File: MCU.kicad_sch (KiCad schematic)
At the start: 3 parts, among them U1 ESP32-S2-SOLO-N4

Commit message: Completed first iteration and reviews
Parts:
- added GND1: TestPoint, TestPoint:TestPoint_Pad_D1.0mm, symbol Connector:TestPoint
- added J3: Conn_02x03_Odd_Even, Connector_PinHeader_1.27mm:PinHeader_2x03_P1.27mm_Vertical_SMD, symbol Connector_Generic:Conn_02x03_Odd_Even
- added R2, R5: 10k, Resistor_SMD:R_0805_2012Metric_Pad1.20x1.40mm_HandSolder, symbol Device:R
- C1: footprint (none) -> Capacitor_SMD:C_0805_2012Metric_Pad1.18x1.45mm_HandSolder; Supplier (none) -> Digikey; Supplier Part Number (none) -> 1276-CL21A226MAYNNNECT-ND
- C2: footprint (none) -> Capacitor_SMD:C_0805_2012Metric_Pad1.18x1.45mm_HandSolder; Supplier (none) -> Digikey; Supplier Part Number (none) -> 1276-1003-1-ND
- U1: value ESP32-S2-SOLO-N4 -> ESP32-S2-SOLO-2-N4; footprint ESP32-S2-SOLO-N4:XCVR_ESP32-S2-SOLO-N4 -> Hydro_footprints:ESP32-S2-SOLO-N4; Supplier (none) -> Digikey; Supplier Part Number (none) -> 1965-ESP32-S2-SOLO-2-N4CT-ND
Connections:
- net GND: now also GND1.1, J3.4 (Pin_4)
- net OP_AMP_POWER: now also U1.17 (IO9); no longer U1.6 (IO6)
- net SENSOR_OUTPUT: now also U1.18 (IO10); no longer U1.4 (IO4)
- net SENSOR_PWR: now also U1.19 (IO11); no longer U1.7 (IO7)
- net 3V3: now reaches C1.1, C2.1, U1.2 (3V3)
- net 3V3: now also J3.2 (Pin_2), R2.1, R5.1
- net QI_EN2: now reaches U1.10 (IO17)
- net CHARGE_STATUS: now reaches U1.11 (IO18)
- net Battery_Voltage: now reaches U1.12 (IO8)
- net ESP_BOOT: now reaches U1.27 (IO0)
- net ESP_BOOT: now also J3.6 (Pin_6), R5.2
- net ESP_EN: now reaches U1.3 (EN)
- net ESP_EN: now also J3.1 (Pin_1), R2.2
- net RXD0: now reaches U1.36 (RXD0)
- net RXD0: now also J3.5 (Pin_5)
- net TXD0: now reaches U1.37 (TXD0)
- net TXD0: now also J3.3 (Pin_3)
- no-connect marks 0 -> 27
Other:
- note added: "Ensure to pullup on MCU"
- company: (none) -> Horatio Pistachio
- title: (none) -> WashingLineMonitor-P0001
- moved on the sheet: C1, C2

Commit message: commit of local files before designing next version
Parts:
- J3: Digikey_Part_Number (none) -> SAM13920TR-ND; Part_Number SAM13920TR-ND -> (none)
- U1: JLC_Part_Number (none) -> C3040594
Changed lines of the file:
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@@
+			)
+		)
+		(property "JLC_Part_Number" ""
+			(at 175.26 77.47 0)
+			(effects
+				(font
+					(size 1.27 1.27)
+				)
+				(hide yes)
 			)
 		)
@@
 			)
 		)
-		(property "Part_Number" "SAM13920TR-ND"
-			(at 41.91 176.53 0)
-			(effects
-				(font
-					(size 1.27 1.27)
-				)
-				(hide yes)
-			)
-		)
 		(property "Supplier" "Digikey"
 			(at 41.91 176.53 0)
@@
 		)
 		(property "Supplier Part Number" "SAM13920TR-ND"
+			(at 41.91 176.53 0)
+			(effects
+				(font
+					(size 1.27 1.27)
+				)
+				(hide yes)
+			)
+		)
+		(property "Digikey_Part_Number" "SAM13920TR-ND"
+			(at 41.91 176.53 0)
+			(effects
+				(font
+					(size 1.27 1.27)
+				)
+				(hide yes)
+			)
+		)
+		(property "JLC_Part_Number" ""
 			(at 41.91 176.53 0)
 			(effects
@@
 			)
 		)
+		(property "JLC_Part_Number" ""
+			(at 105.41 63.5 0)
+			(effects
+				(font
+					(size 1.27 1.27)
+				)
+				(hide yes)
+			)
+		)
 		(pin "1"
 		)
@@
 			)
 		)
+		(property "JLC_Part_Number" "C3040594"
+			(at 125.73 96.52 0)
+			(effects
+				(font
+					(size 1.27 1.27)
+				)
+				(hide yes)
+			)
+		)
 		(pin "38"
 		)
@@
 			)
 		)
+		(property "JLC_Part_Number" ""
+			(at 82.55 64.77 0)
+			(effects
+				(font
+					(size 1.27 1.27)
+				)
+				(hide yes)
+			)
+		)
 		(pin "1"
 		)
@@
 			)
 		)
+		(property "JLC_Part_Number" ""
+			(at 149.86 124.46 0)
+			(effects
+				(font
+					(size 1.27 1.27)
+				)
+				(hide yes)
+			)
+		)
 		(pin "1"
 		)
@@
 			(at 187.96 77.47 0)
 			(effects
+				(font
+					(size 1.27 1.27)
+				)
+				(hide yes)
+			)
+		)
+		(property "JLC_Part_Number" ""
+			(at 187.96 77.47 0)
+			(effects

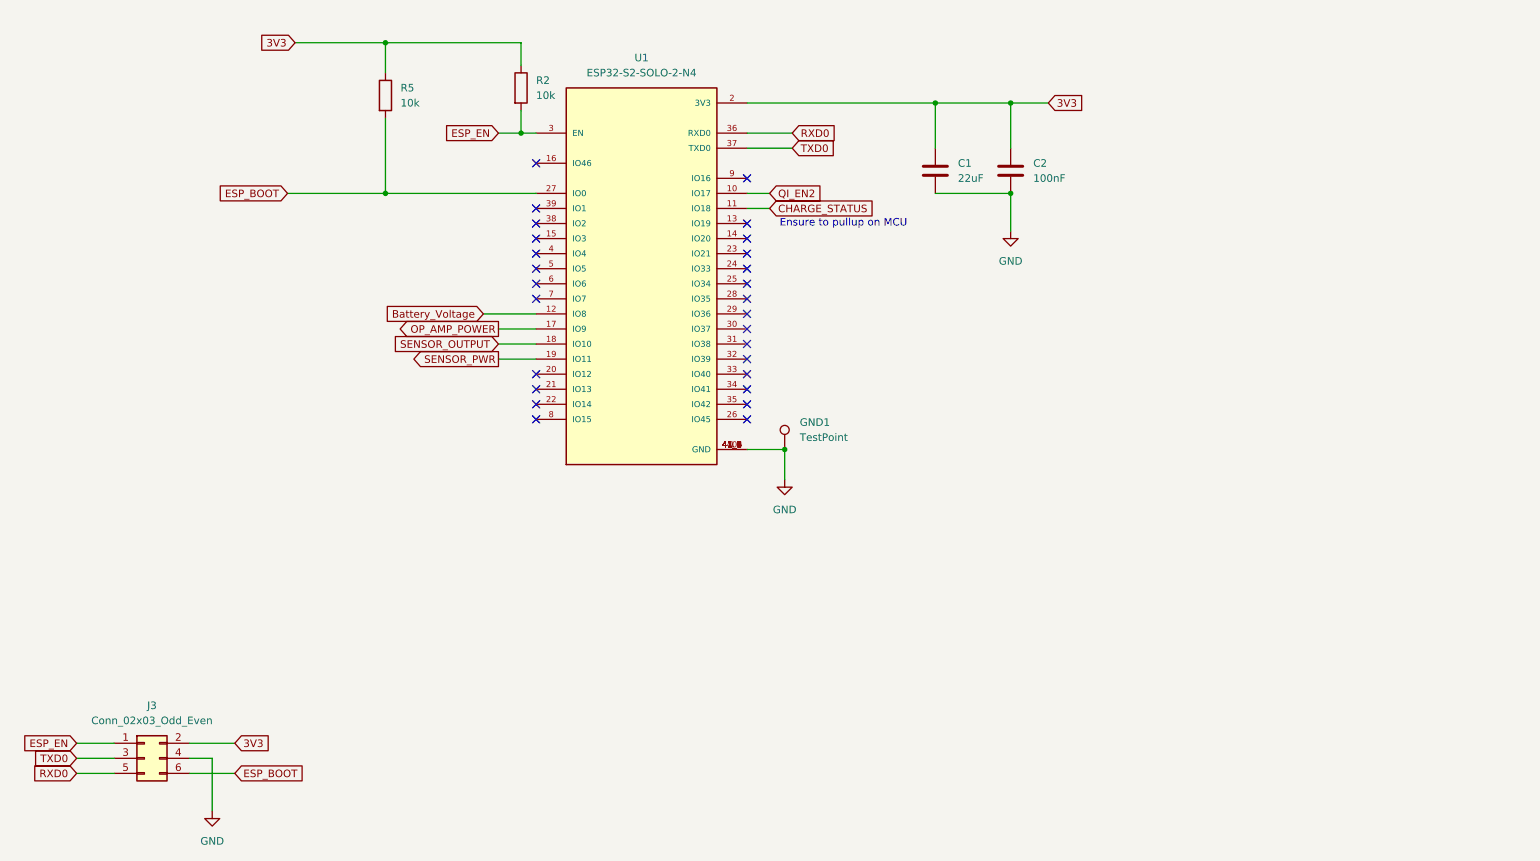
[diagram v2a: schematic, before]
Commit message: updated schematic from review
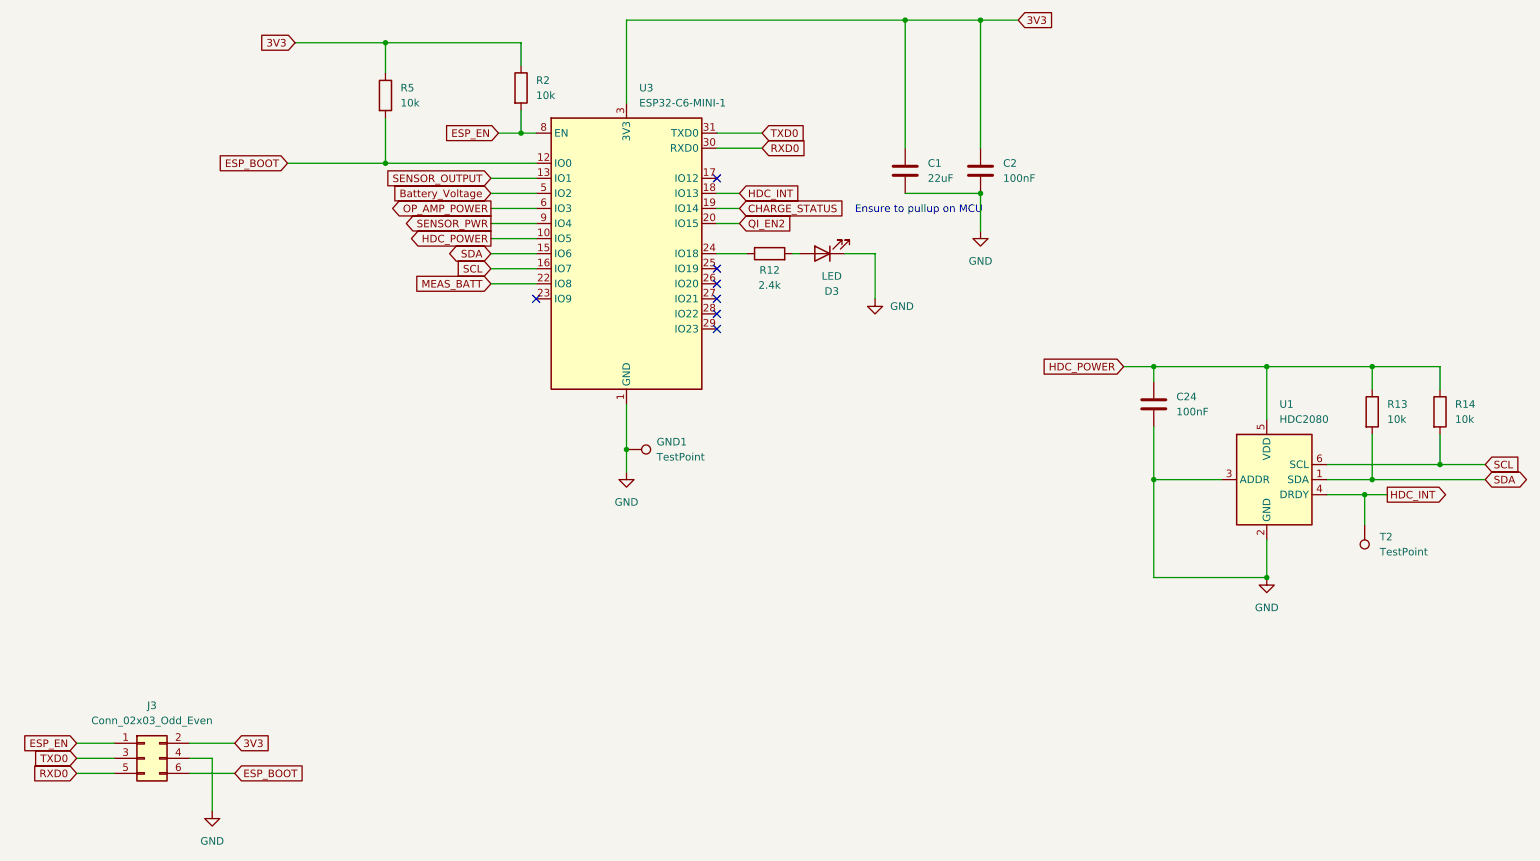
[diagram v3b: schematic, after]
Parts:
- removed U1: ESP32-S2-SOLO-2-N4, Hydro_footprints:ESP32-S2-SOLO-N4, symbol Hydro_symbols:ESP32-S2-SOLO-N4
- added C24: 100nF, Capacitor_SMD:C_0805_2012Metric_Pad1.18x1.45mm_HandSolder, symbol Device:C
- added D3: LED, LED_SMD:LED_0805_2012Metric_Pad1.15x1.40mm_HandSolder, symbol Device:LED
- added R12: 2.4k, Resistor_SMD:R_0805_2012Metric_Pad1.20x1.40mm_HandSolder, symbol Device:R
- added R13, R14: 10k, Resistor_SMD:R_0805_2012Metric_Pad1.20x1.40mm_HandSolder, symbol Device:R
- added T2: TestPoint, TestPoint:TestPoint_Pad_D1.0mm, symbol Connector:TestPoint
- added U1: HDC2080, Sensor_Humidity:Texas_S-PWSON-N6-HDC2080, symbol Sensor_Humidity:HDC2080
- added U3: ESP32-C6-MINI-1, RF_Module:ESP32-C6-MINI-1, symbol RF_Module:ESP32-C6-MINI-1
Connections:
- net 3V3: now also U3.3 (3V3)
- net Battery_Voltage: now also U3.5 (IO2)
- net CHARGE_STATUS: now also U3.19 (IO14)
- net ESP_BOOT: now also U3.12 (IO0)
- net ESP_EN: now also U3.8 (EN)
- net GND: now also C24.2, D3.1 (K), U1.2 (GND), U1.3 (ADDR), U3.1 (GND), U3.11 (GND), U3.14 (GND), U3.2 (GND), U3.36 (GND), U3.37 (GND), U3.38 (GND), U3.39 (GND), U3.40 (GND), U3.41 (GND), U3.42 (GND), U3.43 (GND), U3.44 (GND), U3.45 (GND), U3.46 (GND), U3.47 (GND), U3.48 (GND), U3.49 (GND), U3.50 (GND), U3.51 (GND), U3.52 (GND), U3.53 (GND)
- net OP_AMP_POWER: now also U3.6 (IO3)
- net QI_EN2: now also U3.20 (IO15)
- net RXD0: now also U3.30 (RXD0)
- net SENSOR_OUTPUT: now also U3.13 (IO1)
- net SENSOR_PWR: now also U3.9 (IO4)
- net TXD0: now also U3.31 (TXD0)
- new net: R12.1, U3.24 (IO18)
- new net: D3.2 (A), R12.2
- new net HDC_INT: T2.1, U1.4 (DRDY), U3.18 (IO13)
- new net HDC_POWER: C24.1, R13.1, R14.1, U1.5 (VDD), U3.10 (IO5)
- new net MEAS_BATT: U3.22 (IO8)
- new net SCL: R14.2, U1.6 (SCL), U3.16 (IO7)
- new net SDA: R13.2, U1.1 (SDA), U3.15 (IO6)
- no-connect marks 27 -> 7
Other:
- moved on the sheet: C1, C2, GND1

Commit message: laid out pcb
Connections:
- net CHARGE_STATUS: now also U3.20 (IO15); no longer U3.19 (IO14)
- net HDC_POWER: now also U3.13 (IO1); no longer U3.10 (IO5)
- net OP_AMP_POWER: now also U3.10 (IO5); no longer U3.6 (IO3)
- net QI_EN2: now also U3.19 (IO14); no longer U3.20 (IO15)
- net SENSOR_OUTPUT: now also U3.9 (IO4); no longer U3.13 (IO1)
- net SENSOR_PWR: now also U3.6 (IO3); no longer U3.9 (IO4)

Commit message: Near complete AC
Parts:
- renumbered GND1 to TP3, T2 to TP4
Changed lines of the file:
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@@
 		(dnp no)
 		(fields_autoplaced yes)
-		(property "Reference" "T2"
+		(property "Reference" "TP4"
 			(at 250.19 139.1919 0)
 			(show_name no)
@@
 			(project "WashingLineMonitor-P0001"
 				(path "/09468f75-1295-4aed-9d66-1cbb46f6d9f7/e08ac9de-dc6d-4cae-9407-56af78bc3f75"
-					(reference "T2")
+					(reference "TP4")
 					(unit 1)
 				)
@@
 		(dnp no)
 		(fields_autoplaced yes)
-		(property "Reference" "GND1"
+		(property "Reference" "TP3"
 			(at 128.27 123.1899 90)
 			(show_name no)
@@
 			(project "WashingLineMonitor-P0001"
 				(path "/09468f75-1295-4aed-9d66-1cbb46f6d9f7/e08ac9de-dc6d-4cae-9407-56af78bc3f75"
-					(reference "GND1")
+					(reference "TP3")
 					(unit 1)
 				)

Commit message: Minor pre release changes
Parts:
- TP3, TP4: now left out of the parts list
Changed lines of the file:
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@@
 	(title_block
 		(title "WashingLineMonitor-P0001")
-		(date "2025-09-14")
-		(rev "AB")
+		(date "2026-06-06")
+		(rev "AC")
 		(company "Horatio Pistachio")
 	)
@@
 		(body_style 1)
 		(exclude_from_sim no)
-		(in_bom yes)
+		(in_bom no)
 		(on_board yes)
 		(in_pos_files yes)
@@
 		(body_style 1)
 		(exclude_from_sim no)
-		(in_bom yes)
+		(in_bom no)
 		(on_board yes)
 		(in_pos_files yes)
